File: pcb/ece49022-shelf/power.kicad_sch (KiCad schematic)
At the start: 16 parts, among them U2 TPS54202DDCT, U4 NCP1117-3.3_SOT223

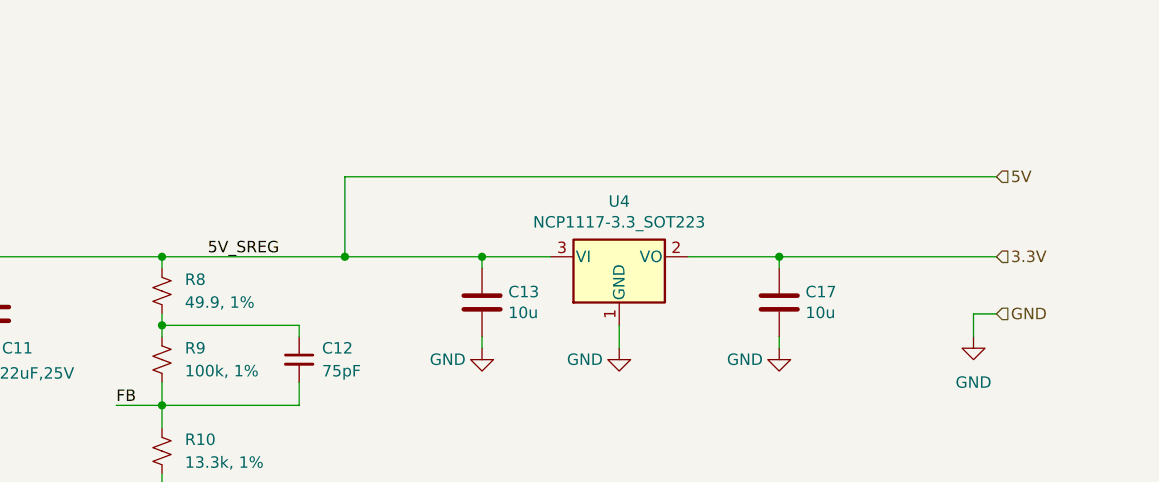
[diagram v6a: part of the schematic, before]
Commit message: new converter layout
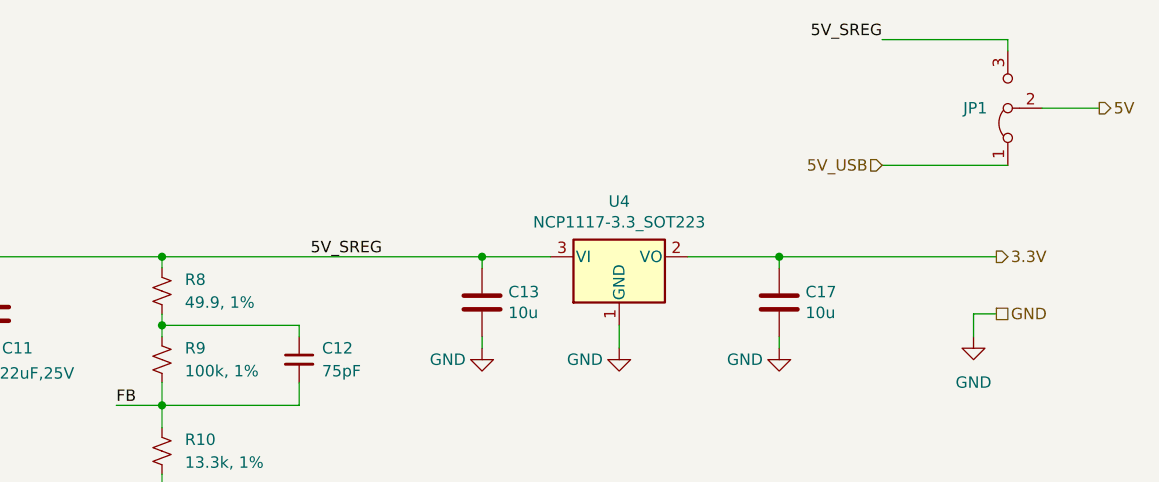
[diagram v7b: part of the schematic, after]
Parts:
- added JP1: Jumper_3_Bridged12, Connector_PinHeader_2.54mm:PinHeader_1x03_P2.54mm_Vertical, symbol Jumper:Jumper_3_Bridged12
- C7: footprint Capacitor_SMD:C_0805_2012Metric_Pad1.18x1.45mm_HandSolder -> Capacitor_SMD:C_1206_3216Metric
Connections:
- net 5V: now also JP1.2 (C); no longer C10.1, C11.1, C13.1, L2.2, R8.1, U4.3 (VI)
- new net 5V_SREG: C10.1, C11.1, C13.1, JP1.3 (B), L2.2, R8.1, U4.3 (VI)
- new net 5V_USB: JP1.1 (A)
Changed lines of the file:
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@@
-	)
-	(junction
-		(at 165.1 87.63)
-		(diameter 0)
-		(color 0 0 0 0)
 	)
 	(junction
@@
 	(wire
 		(pts
-			(xy 165.1 87.63) (xy 180.34 87.63)
+			(xy 144.78 87.63) (xy 180.34 87.63)
 		)
 		(stroke
@@
 	(wire
 		(pts
-			(xy 165.1 78.74) (xy 237.49 78.74)
-		)
-		(stroke
-			(width 0)
-			(type default)
-		)
-	)
-	(wire
-		(pts
 			(xy 144.78 111.76) (xy 144.78 114.3)
 		)
@@
 	(wire
 		(pts
-			(xy 165.1 78.74) (xy 165.1 87.63)
-		)
-		(stroke
-			(width 0)
-			(type default)
-		)
-	)
-	(wire
-		(pts
 			(xy 213.36 87.63) (xy 237.49 87.63)
 		)
@@
 	(wire
 		(pts
+			(xy 224.79 63.5) (xy 238.76 63.5)
+		)
+		(stroke
+			(width 0)
+			(type default)
+		)
+	)
+	(wire
+		(pts
 			(xy 81.28 81.28) (xy 83.82 81.28)
 		)
@@
 	(wire
 		(pts
+			(xy 224.79 77.47) (xy 238.76 77.47)
+		)
+		(stroke
+			(width 0)
+			(type default)
+		)
+	)
+	(wire
+		(pts
 			(xy 38.1 95.25) (xy 45.72 95.25)
 		)
@@
 	(wire
 		(pts
+			(xy 238.76 63.5) (xy 238.76 64.77)
+		)
+		(stroke
+			(width 0)
+			(type default)
+		)
+	)
+	(wire
+		(pts
 			(xy 63.5 104.14) (xy 63.5 107.95)
 		)
@@
 	(wire
 		(pts
+			(xy 242.57 71.12) (xy 248.92 71.12)
+		)
+		(stroke
+			(width 0)
+			(type default)
+		)
+	)
+	(wire
+		(pts
 			(xy 27.94 82.55) (xy 27.94 91.44)
 		)
@@
 	(wire
 		(pts
-			(xy 144.78 87.63) (xy 165.1 87.63)
-		)
-		(stroke
-			(width 0)
-			(type default)
-		)
-	)
-	(wire
-		(pts
 			(xy 27.94 99.06) (xy 27.94 106.68)
 		)
@@
 			(width 0)
 			(type default)
+		)
+	)
+	(label "5V_SREG"
+		(at 224.79 63.5 180)
+		(effects
+			(font
+				(size 1.27 1.27)
+			)
+			(justify right bottom)
 		)
 	)
@@
 	)
 	(label "5V_SREG"
-		(at 149.86 87.63 0)
+		(at 161.29 87.63 0)
 		(effects
 			(font
@@
 	)
 	(hierarchical_label "5V"
-		(shape input)
-		(at 237.49 78.74 0)
+		(shape output)
+		(at 248.92 71.12 0)
 		(effects
 			(font
@@
 	)
 	(hierarchical_label "3.3V"
-		(shape input)
+		(shape output)
 		(at 237.49 87.63 0)
 		(effects
@@
 	)
 	(hierarchical_label "GND"
-		(shape input)
+		(shape passive)
 		(at 237.49 93.98 0)
 		(effects
@@
 			)
 			(justify left)
+		)
+	)
+	(hierarchical_label "5V_USB"
+		(shape input)
+		(at 224.79 77.47 180)
+		(effects
+			(font
+				(size 1.27 1.27)
+			)
+			(justify right)
 		)
 	)
@@
 	)
 	(symbol
+		(lib_id "Jumper:Jumper_3_Bridged12")
+		(at 238.76 71.12 90)
+		(unit 1)
+		(exclude_from_sim no)
+		(in_bom yes)
+		(on_board yes)
+		(dnp no)
+		(property "Reference" "JP1"
+			(at 236.474 71.12 90)
+			(effects
+				(font
+					(size 1.27 1.27)
+				)
+				(justify left)
+			)
+		)
+		(property "Value" "Jumper_3_Bridged12"
+			(at 236.22 72.3899 90)
+			(effects
+				(font
+					(size 1.27 1.27)
+				)
+				(justify left)
+				(hide yes)
+			)
+		)
+		(property "Footprint" "Connector_PinHeader_2.54mm:PinHeader_1x03_P2.54mm_Vertical"
+			(at 238.76 71.12 0)
+			(effects
+				(font
+					(size 1.27 1.27)
+				)
+				(hide yes)
+			)
+		)
+		(property "Datasheet" "~"
+			(at 238.76 71.12 0)
+			(effects
+				(font
+					(size 1.27 1.27)
+				)
+				(hide yes)
+			)
+		)
+		(property "Description" "Jumper, 3-pole, pins 1+2 closed/bridged"
+			(at 238.76 71.12 0)
+			(effects
+				(font
+					(size 1.27 1.27)
+				)
+				(hide yes)
+			)
+		)
+		(pin "2"
+		)
+		(pin "3"
+		)
+		(pin "1"
+		)
+		(instances
+			(project ""
+				(path "/cb6cb1b4-c151-4aa2-8cd7-5430288cfa02/8caba1e8-90c1-45e5-9cde-4efd1c8301b8"
+					(reference "JP1")
+					(unit 1)
+				)
+			)
+		)
+	)
+	(symbol
 		(lib_id "power:GND")
 		(at 33.02 107.95 0)
@@
 			)
 		)
-		(property "Footprint" "Capacitor_SMD:C_0805_2012Metric_Pad1.18x1.45mm_HandSolder"
+		(property "Footprint" "Capacitor_SMD:C_1206_3216Metric"
 			(at 28.9052 99.06 0)
 			(effects

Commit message: stuff
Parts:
- added D1: LED, Resistor_SMD:R_0603_1608Metric, symbol Device:LED
- added R12: 100, Resistor_SMD:R_0603_1608Metric, symbol Device:R_Small_US
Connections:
- net 3.3V: now also R12.1
- net GND: now also D1.1 (K)
- new net: D1.2 (A), R12.2
